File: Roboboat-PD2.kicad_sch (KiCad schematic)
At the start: 37 parts, among them J1 14.4V, J10 Motor, J11 Motor, J12 Motor, J13 Motor, J14 Motor, J15 Motor, J16 Motor, J17 GND TP, J2 PGOOD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

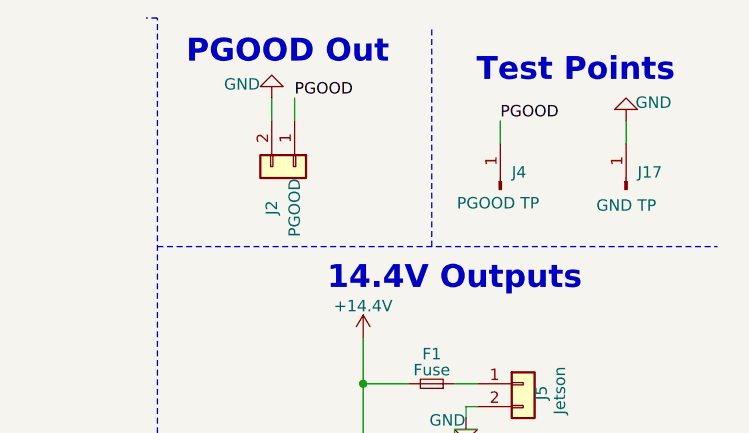
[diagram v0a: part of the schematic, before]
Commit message: add 0.1uF capacitors to PGOOD output
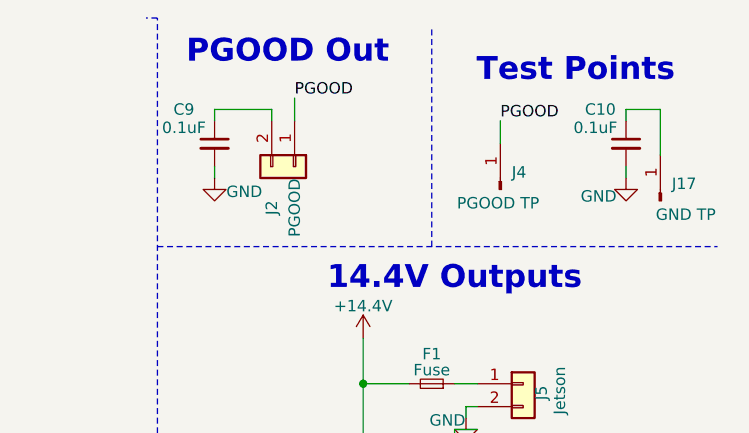
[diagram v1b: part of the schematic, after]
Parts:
- added C10, C9: 0.1uF, Capacitor_SMD:C_0805_2012Metric, symbol Device:C_Small
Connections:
- net GND: now also C10.2, C9.2; no longer J17.1 (Pin_1), J2.2 (Pin_2)
- new net: C9.1, J2.2 (Pin_2)
- new net: C10.1, J17.1 (Pin_1)
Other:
- moved on the sheet: J17
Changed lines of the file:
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@@
 	(wire
 		(pts
+			(xy 234.95 21.59) (xy 234.95 22.86)
+		)
+		(stroke
+			(width 0)
+			(type default)
+		)
+	)
+	(wire
+		(pts
 			(xy 170.18 76.2) (xy 173.99 76.2)
 		)
@@
 	(wire
 		(pts
+			(xy 274.32 21.59) (xy 278.13 21.59)
+		)
+		(stroke
+			(width 0)
+			(type default)
+		)
+	)
+	(wire
+		(pts
 			(xy 254 105.41) (xy 254 114.3)
 		)
@@
 	(wire
 		(pts
+			(xy 228.6 21.59) (xy 234.95 21.59)
+		)
+		(stroke
+			(width 0)
+			(type default)
+		)
+	)
+	(wire
+		(pts
 			(xy 237.49 20.32) (xy 237.49 22.86)
 		)
@@
 	(wire
 		(pts
+			(xy 274.32 22.86) (xy 274.32 21.59)
+		)
+		(stroke
+			(width 0)
+			(type default)
+		)
+	)
+	(wire
+		(pts
 			(xy 172.72 100.33) (xy 172.72 104.14)
 		)
@@
 	(wire
 		(pts
+			(xy 228.6 22.86) (xy 228.6 21.59)
+		)
+		(stroke
+			(width 0)
+			(type default)
+		)
+	)
+	(wire
+		(pts
 			(xy 247.65 86.36) (xy 247.65 88.9)
 		)
@@
 		)
 	)
+	(wire
+		(pts
+			(xy 278.13 21.59) (xy 278.13 26.67)
+		)
+		(stroke
+			(width 0)
+			(type default)
+		)
+	)
 	(polyline
 		(pts
@@
 	(wire
 		(pts
-			(xy 274.32 22.86) (xy 274.32 25.4)
+			(xy 274.32 29.21) (xy 274.32 27.94)
 		)
 		(stroke
@@
 	(wire
 		(pts
-			(xy 234.95 20.32) (xy 234.95 22.86)
+			(xy 228.6 29.21) (xy 228.6 27.94)
 		)
 		(stroke
@@
 	(symbol
 		(lib_id "power:GND")
-		(at 234.95 20.32 180)
+		(at 228.6 29.21 0)
 		(unit 1)
 		(exclude_from_sim no)
@@
 		(dnp no)
 		(property "Reference" "#PWR015"
-			(at 234.95 13.97 0)
+			(at 228.6 35.56 0)
 			(effects
 				(font
@@
 		)
 		(property "Value" "GND"
-			(at 231.648 18.796 0)
+			(at 231.902 30.734 0)
 			(effects
 				(font
@@
 		)
 		(property "Footprint" ""
-			(at 234.95 20.32 0)
+			(at 228.6 29.21 0)
 			(effects
 				(font
@@
 		)
 		(property "Datasheet" ""
-			(at 234.95 20.32 0)
+			(at 228.6 29.21 0)
 			(effects
 				(font
@@
 		)
 		(property "Description" "Power symbol creates a global label with name \"GND\" , ground"
-			(at 234.95 20.32 0)
+			(at 228.6 29.21 0)
 			(effects
 				(font
@@
 	)
 	(symbol
+		(lib_id "Device:C_Small")
+		(at 228.6 25.4 0)
+		(unit 1)
+		(exclude_from_sim no)
+		(in_bom yes)
+		(on_board yes)
+		(dnp no)
+		(property "Reference" "C9"
+			(at 224.028 21.59 0)
+			(effects
+				(font
+					(size 1.27 1.27)
+				)
+				(justify left)
+			)
+		)
+		(property "Value" "0.1uF"
+			(at 222.758 23.622 0)
+			(effects
+				(font
+					(size 1.27 1.27)
+				)
+				(justify left)
+			)
+		)
+		(property "Footprint" "Capacitor_SMD:C_0805_2012Metric"
+			(at 228.6 25.4 0)
+			(effects
+				(font
+					(size 1.27 1.27)
+				)
+				(hide yes)
+			)
+		)
+		(property "Datasheet" "~"
+			(at 228.6 25.4 0)
+			(effects
+				(font
+					(size 1.27 1.27)
+				)
+				(hide yes)
+			)
+		)
+		(property "Description" "Unpolarized capacitor, small symbol"
+			(at 228.6 25.4 0)
+			(effects
+				(font
+					(size 1.27 1.27)
+				)
+				(hide yes)
+			)
+		)
+		(pin "2"
+		)
+		(pin "1"
+		)
+		(instances
+			(project "Roboboat-PD2"
+				(path "/9a1496f4-7cef-4d33-8239-9c2f43ceb177"
+					(reference "C9")
+					(unit 1)
+				)
+			)
+		)
+	)
+	(symbol
 		(lib_id "power:GND")
 		(at 121.92 74.93 0)
@@
 	(symbol
 		(lib_id "Connector:Conn_01x01_Pin")
-		(at 274.32 30.48 90)
+		(at 278.13 31.75 90)
 		(unit 1)
 		(exclude_from_sim no)
@@
 		(dnp no)
 		(property "Reference" "J17"
-			(at 275.59 28.5749 90)
+			(at 279.4 29.8449 90)
 			(effects
 				(font
@@
 		)
 		(property "Value" "GND TP"
-			(at 271.018 32.258 90)
+			(at 277.622 33.274 90)
 			(effects
 				(font
@@
 		)
 		(property "Footprint" "TestPoint:TestPoint_Keystone_5010-5014_Multipurpose"
-			(at 274.32 30.48 0)
+			(at 278.13 31.75 0)
 			(effects
 				(font
@@
 		)
 		(property "Datasheet" "~"
-			(at 274.32 30.48 0)
+			(at 278.13 31.75 0)
 			(effects
 				(font
@@
 		)
 		(property "Description" "Generic connector, single row, 01x01, script generated"
-			(at 274.32 30.48 0)
+			(at 278.13 31.75 0)
 			(effects
 				(font
@@
 	)
 	(symbol
+		(lib_id "Device:C_Small")
+		(at 274.32 25.4 0)
+		(unit 1)
+		(exclude_from_sim no)
+		(in_bom yes)
+		(on_board yes)
+		(dnp no)
+		(property "Reference" "C10"
+			(at 269.748 21.59 0)
+			(effects
+				(font
+					(size 1.27 1.27)
+				)
+				(justify left)
+			)
+		)
+		(property "Value" "0.1uF"
+			(at 268.478 23.622 0)
+			(effects
+				(font
+					(size 1.27 1.27)
+				)
+				(justify left)
+			)
+		)
+		(property "Footprint" "Capacitor_SMD:C_0805_2012Metric"
+			(at 274.32 25.4 0)
+			(effects
+				(font
+					(size 1.27 1.27)
+				)
+				(hide yes)
+			)
+		)
+		(property "Datasheet" "~"
+			(at 274.32 25.4 0)
+			(effects
+				(font
+					(size 1.27 1.27)
+				)
+				(hide yes)
+			)
+		)
+		(property "Description" "Unpolarized capacitor, small symbol"
+			(at 274.32 25.4 0)
+			(effects
+				(font
+					(size 1.27 1.27)
+				)
+				(hide yes)
+			)
+		)
+		(pin "2"
+		)
+		(pin "1"
+		)
+		(instances
+			(project "Roboboat-PD2"
+				(path "/9a1496f4-7cef-4d33-8239-9c2f43ceb177"
+					(reference "C10")
+					(unit 1)
+				)
+			)
+		)
+	)
+	(symbol
 		(lib_id "Device:R_Small_US")
 		(at 129.54 41.91 0)
@@
 	(symbol
 		(lib_id "power:GND")
-		(at 274.32 22.86 180)
+		(at 274.32 29.21 0)
 		(unit 1)
 		(exclude_from_sim no)
@@
 		(dnp no)
 		(property "Reference" "#PWR031"
-			(at 274.32 16.51 0)
+			(at 274.32 35.56 0)
 			(effects
 				(font
@@
 		)
 		(property "Value" "GND"
-			(at 277.368 20.828 0)
+			(at 271.272 31.242 0)
 			(effects
 				(font
@@
 		)
 		(property "Footprint" ""
-			(at 274.32 22.86 0)
+			(at 274.32 29.21 0)
 			(effects
 				(font
@@
 		)
 		(property "Datasheet" ""
-			(at 274.32 22.86 0)
+			(at 274.32 29.21 0)
 			(effects
 				(font
@@
 		)
 		(property "Description" "Power symbol creates a global label with name \"GND\" , ground"
-			(at 274.32 22.86 0)
+			(at 274.32 29.21 0)
 			(effects
 				(font

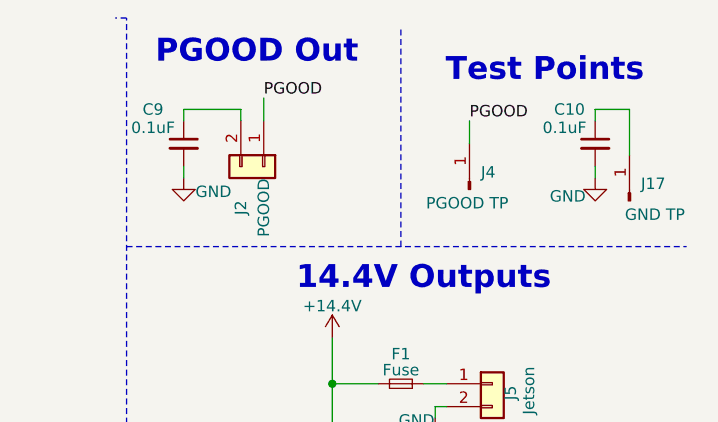
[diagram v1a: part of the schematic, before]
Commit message: add 0.1uF capacitors to PGOOD output
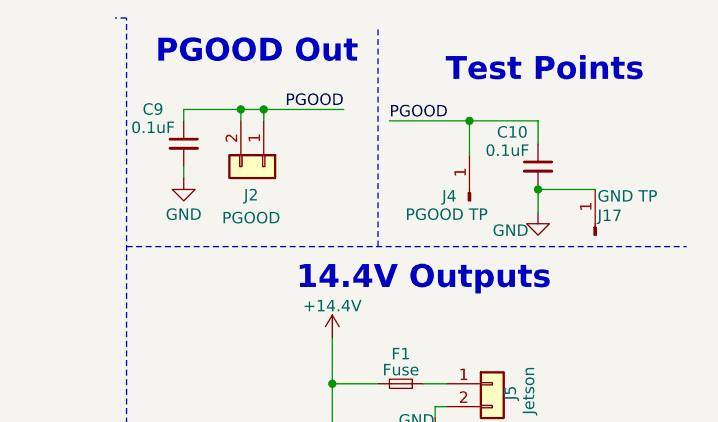
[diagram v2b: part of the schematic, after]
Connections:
- net GND: now also J17.1 (Pin_1)
- net PGOOD: now also C10.1, C9.1, J2.2 (Pin_2)
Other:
- moved on the sheet: J17, J4

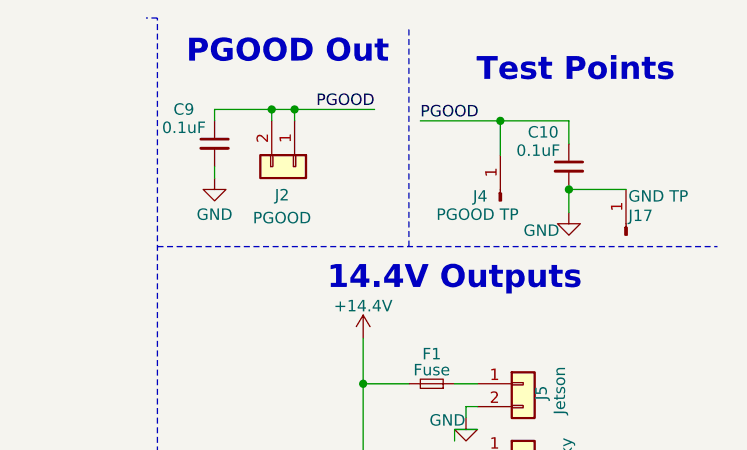
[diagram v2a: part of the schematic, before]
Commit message: redo PCB layout
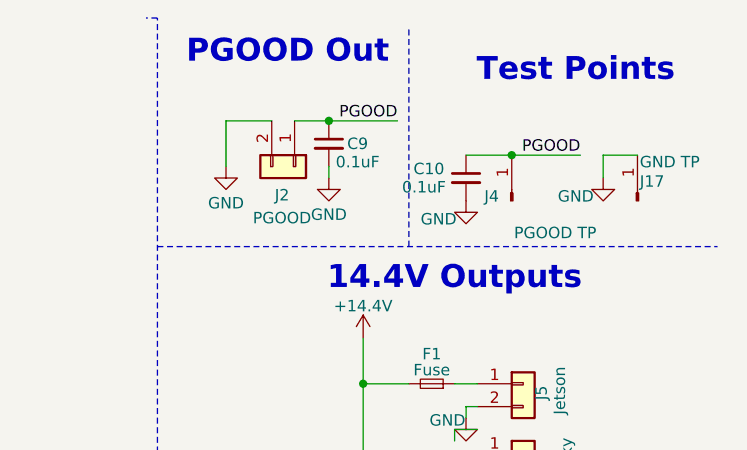
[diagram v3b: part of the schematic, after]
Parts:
- J3, J5: footprint footprints:XT90_V -> Connector_AMASS:AMASS_XT60-M_1x02_P7.20mm_Vertical
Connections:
- net GND: now also J2.2 (Pin_2)
- net PGOOD: no longer J2.2 (Pin_2)
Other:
- moved on the sheet: J17, J4

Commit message: add pullup resistor to PGOOD
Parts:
- removed C10: 0.1uF, Capacitor_SMD:C_0805_2012Metric, symbol Device:C_Small
- added R5: 100k, Resistor_SMD:R_0805_2012Metric, symbol Device:R_Small_US
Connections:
- net GND: no longer C9.2
- net PGOOD: now also C9.2; no longer C9.1, U1.2 (PGOOD)
- net VCC: now reaches C2.1, SW1.2 (B), U1.27 (VCC)
- net VCC: now also R5.1
- new net: C9.1, R5.2, U1.2 (PGOOD)

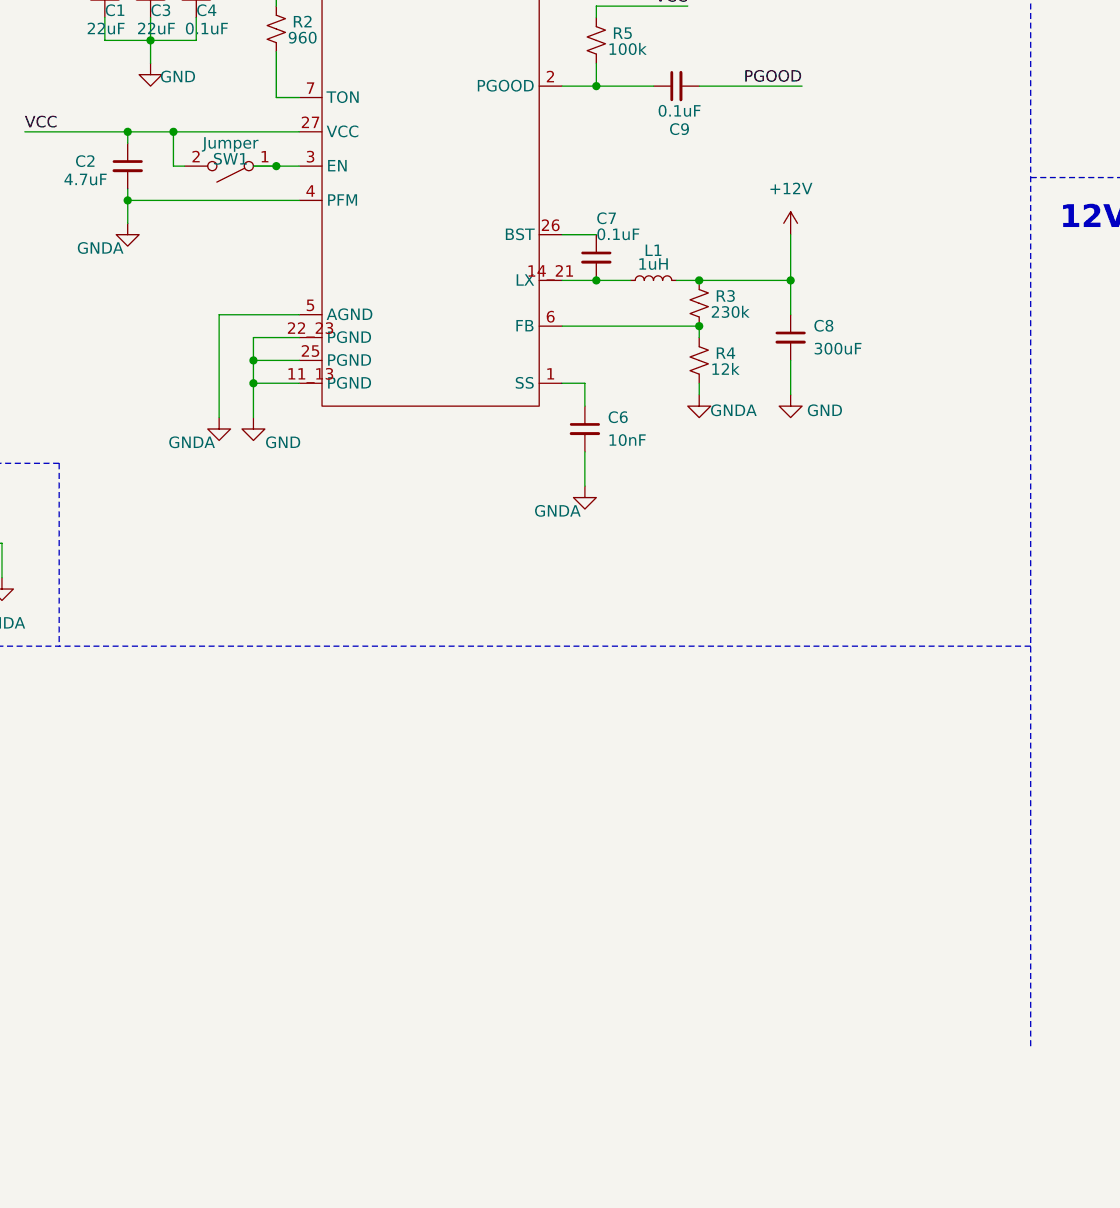
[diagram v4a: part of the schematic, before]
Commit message: add status LEDs
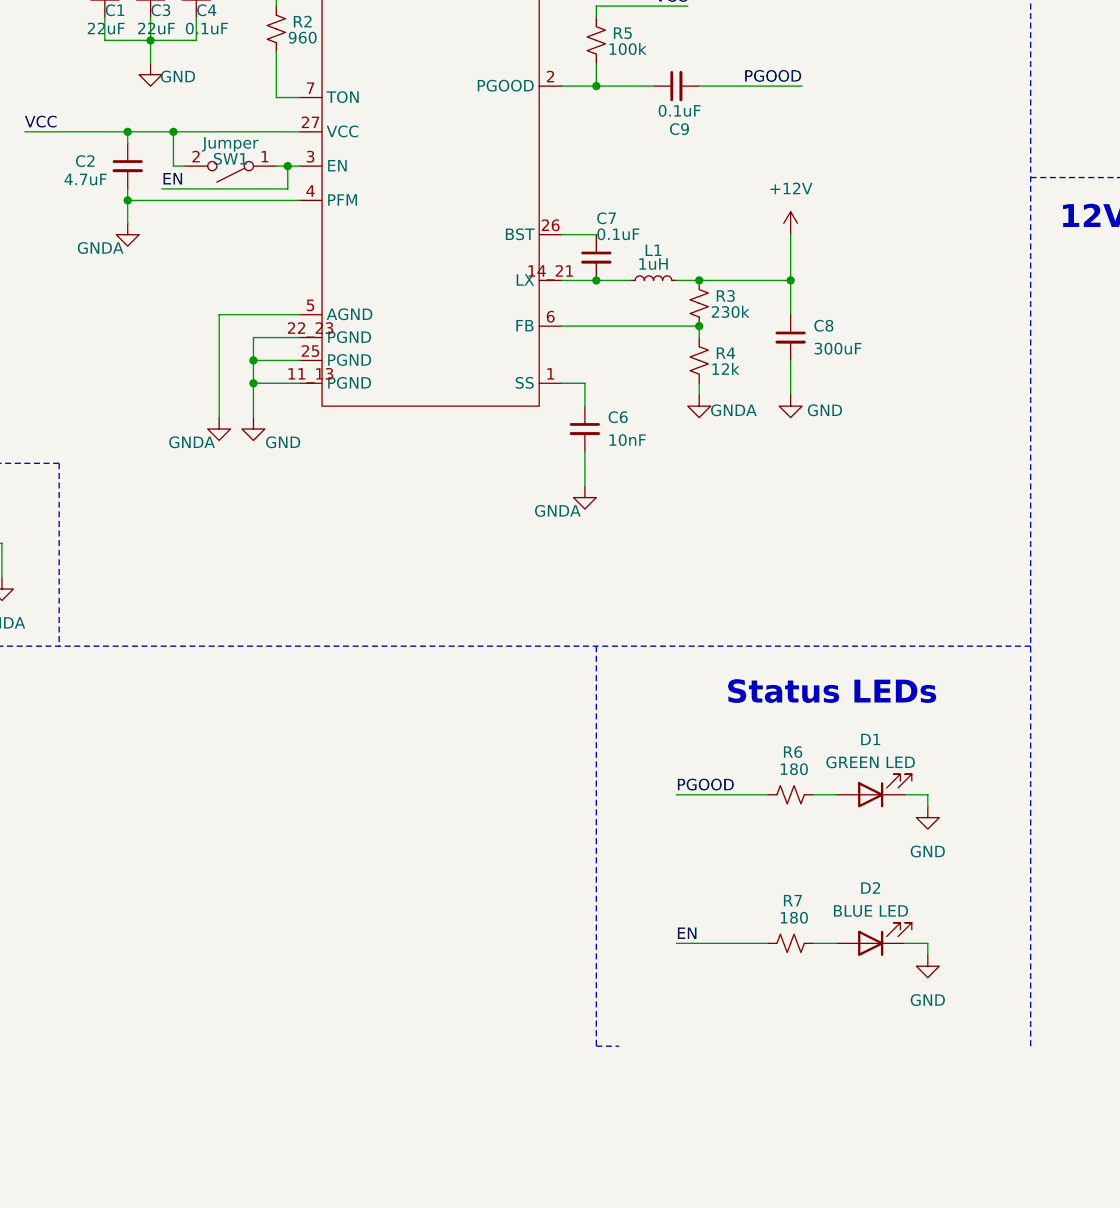
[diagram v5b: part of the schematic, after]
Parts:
- added D1: GREEN LED, LED_THT:LED_D5.0mm, symbol Device:LED
- added D2: BLUE LED, LED_THT:LED_D5.0mm, symbol Device:LED
- added R6, R7: 180, Resistor_SMD:R_0805_2012Metric, symbol Device:R_Small_US
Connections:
- net GND: now also D1.1 (K), D2.1 (K)
- net PGOOD: now also R6.1
- net EN: now reaches SW1.1 (A), U1.3 (EN)
- net EN: now also R7.1
- new net: D2.2 (A), R7.2
- new net: D1.2 (A), R6.2
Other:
- note added: "Status LEDs"
